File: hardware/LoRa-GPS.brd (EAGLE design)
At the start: 50.8 x 17.8 mm, 26 parts, among them J2 MF-CON-MICROUSB-RIGHT, U1 MCP1703-3302E/CB, Y1 CRYSTAL.ABS07

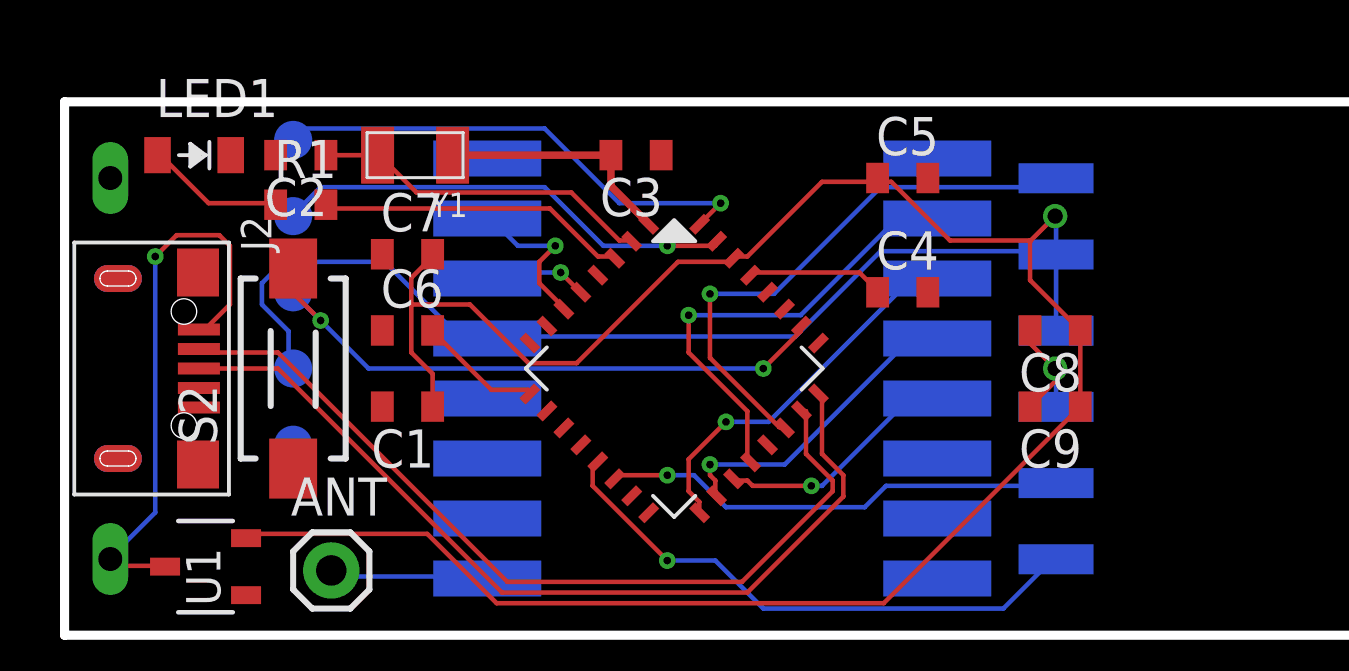
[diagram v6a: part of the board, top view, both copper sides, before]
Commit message: tidy GPS caps routing
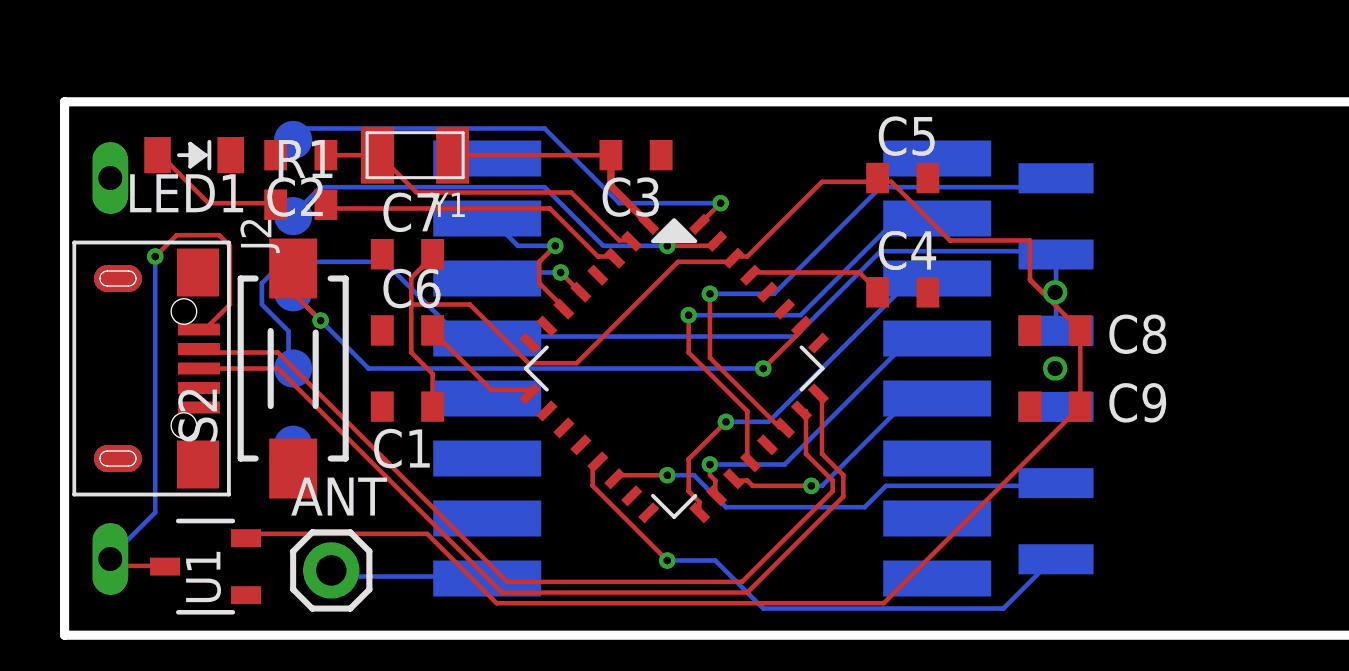
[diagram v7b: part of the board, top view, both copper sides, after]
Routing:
- net GND: track 4.54 -> 0.49 mm
- net VCC: track 105.8 -> 104.3 mm
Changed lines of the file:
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@@
 <layer number="23" name="tOrigins" color="15" fill="1" visible="yes" active="yes"/>
 <layer number="24" name="bOrigins" color="15" fill="1" visible="yes" active="yes"/>
-<layer number="25" name="tNames" color="7" fill="1" visible="no" active="yes"/>
+<layer number="25" name="tNames" color="7" fill="1" visible="yes" active="yes"/>
 <layer number="26" name="bNames" color="7" fill="1" visible="no" active="yes"/>
 <layer number="27" name="tValues" color="7" fill="1" visible="no" active="yes"/>
@@
 </element>
 <element name="LED1" library="nootropicdesign" package="CHIPLED_0805-THINCREAM" value="" x="4.318" y="16.002" smashed="yes" rot="R270">
-<attribute name="NAME" x="3.048" y="17.272" size="1.27" layer="25"/>
+<attribute name="NAME" x="2.032" y="14.097" size="1.27" layer="25"/>
 <attribute name="VALUE" x="3.048" y="13.462" size="1.27" layer="27"/>
 </element>
 <element name="C8" library="nootropicdesign" package="C0603-THINCREAM" value="10uF" x="33.02" y="10.16" smashed="yes" rot="R180">
-<attribute name="NAME" x="33.909" y="9.398" size="1.27" layer="25" rot="R180"/>
+<attribute name="NAME" x="36.83" y="10.668" size="1.27" layer="25" rot="R180"/>
 <attribute name="VALUE" x="33.909" y="12.192" size="1.27" layer="27" rot="R180"/>
 </element>
 <element name="C9" library="nootropicdesign" package="C0603-THINCREAM" value="100nF" x="33.02" y="7.62" smashed="yes" rot="R180">
-<attribute name="NAME" x="33.909" y="6.858" size="1.27" layer="25" rot="R180"/>
+<attribute name="NAME" x="36.83" y="8.382" size="1.27" layer="25" rot="R180"/>
 <attribute name="VALUE" x="33.909" y="9.652" size="1.27" layer="27" rot="R180"/>
 </element>
@@
 </polygon>
 <wire x1="32.1818" y1="10.16" x2="32.1818" y2="9.7282" width="0.1524" layer="1"/>
-<wire x1="32.1818" y1="9.7282" x2="33.02" y2="8.89" width="0.1524" layer="1"/>
-<wire x1="33.02" y1="8.89" x2="33.02" y2="8.4582" width="0.1524" layer="1"/>
-<wire x1="33.02" y1="8.4582" x2="32.1818" y2="7.62" width="0.1524" layer="1"/>
 <wire x1="33.02" y1="8.89" x2="33.05" y2="8.86" width="0.1524" layer="16"/>
-<wire x1="33.05" y1="8.86" x2="33.05" y2="7.61" width="0.1524" layer="16"/>
 </signal>
 <signal name="VCC">
@@
 <contactref element="SAMD21" pad="30"/>
 <contactref element="TP2" pad="P$1"/>
-<wire x1="33.02" y1="13.97" x2="32.1818" y2="13.1318" width="0.1524" layer="1"/>
-<via x="33.02" y="13.97" extent="1-16" drill="0.508"/>
-<wire x1="33.02" y1="13.97" x2="33.05" y2="13.94" width="0.254" layer="16"/>
-<wire x1="33.05" y1="13.94" x2="33.05" y2="12.69" width="0.1524" layer="16"/>
-<wire x1="33.05" y1="12.69" x2="33.05" y2="10.15" width="0.1524" layer="16"/>
+<wire x1="33.02" y1="11.43" x2="32.6136" y2="11.43" width="0.1524" layer="1"/>
+<wire x1="32.6136" y1="11.43" x2="32.1818" y2="11.8618" width="0.1524" layer="1"/>
+<via x="33.02" y="11.43" extent="1-16" drill="0.508"/>
+<wire x1="33.05" y1="11.46" x2="33.02" y2="11.43" width="0.254" layer="16"/>
 <wire x1="12.2682" y1="8.7122" x2="12.2682" y2="7.62" width="0.1524" layer="1"/>
 <wire x1="11.557" y1="9.4234" x2="12.2682" y2="8.7122" width="0.1524" layer="1"/>
@@
 <wire x1="32.1818" y1="13.1572" x2="29.5148" y2="13.1572" width="0.1524" layer="1"/>
 <wire x1="27.2034" y1="15.113" x2="27.1018" y2="15.24" width="0.1524" layer="1"/>
-<wire x1="32.1818" y1="13.1572" x2="32.1818" y2="13.1318" width="0.1524" layer="1"/>
-<wire x1="32.1818" y1="13.1318" x2="32.1818" y2="11.8364" width="0.1524" layer="1"/>
+<wire x1="32.1818" y1="11.8364" x2="32.1818" y2="11.8618" width="0.1524" layer="1"/>
+<wire x1="32.1818" y1="13.1572" x2="32.1818" y2="11.8618" width="0.1524" layer="1"/>
 <wire x1="32.1818" y1="11.8364" x2="33.8582" y2="10.16" width="0.1524" layer="1"/>
 <wire x1="27.305" y1="1.0668" x2="33.8582" y2="7.62" width="0.1524" layer="1"/>
 <wire x1="33.8582" y1="7.62" x2="33.8582" y2="10.16" width="0.1524" layer="1"/>
+<wire x1="33.05" y1="12.69" x2="33.05" y2="11.46" width="0.1524" layer="16"/>
+<wire x1="33.02" y1="11.43" x2="33.05" y2="11.4" width="0.1524" layer="16"/>
+<wire x1="33.05" y1="11.4" x2="33.05" y2="10.15" width="0.1524" layer="16"/>
 </signal>
 <signal name="VIN">
@@
 <wire x1="19.3802" y1="13.8684" x2="19.45505625" y2="13.728909375" width="0.1524" layer="1"/>
 <wire x1="19.45505625" y1="13.728909375" x2="19.47146875" y2="13.698325" width="0.1524" layer="1"/>
-<wire x1="12.934" y1="16.002" x2="18.2118" y2="16.002" width="0.254" layer="1"/>
+<wire x1="12.934" y1="16.002" x2="18.2118" y2="16.002" width="0.1524" layer="1"/>
 <wire x1="18.2118" y1="16.002" x2="18.2118" y2="14.972165625" width="0.254" layer="1"/>
 <wire x1="18.2118" y1="14.972165625" x2="19.45505625" y2="13.728909375" width="0.254" layer="1"/>

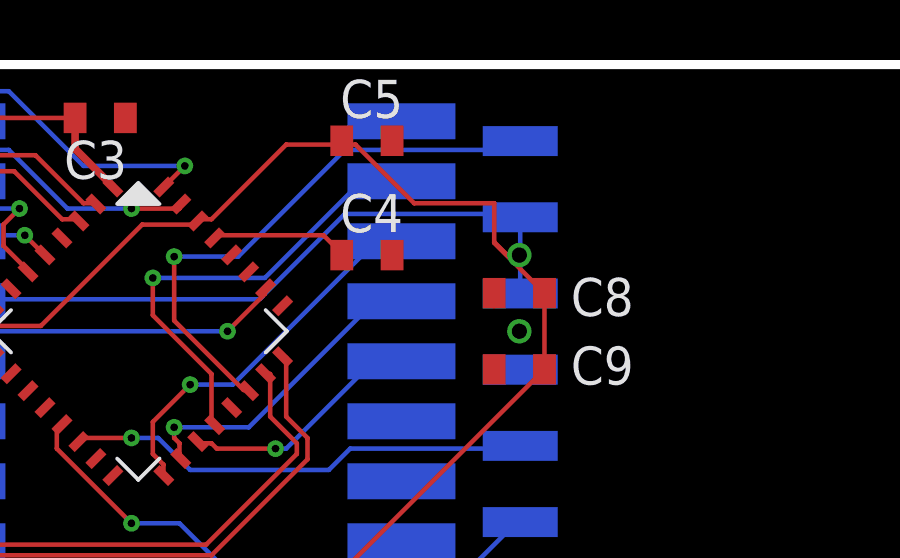
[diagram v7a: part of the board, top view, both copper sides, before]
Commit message: all vias 0.01
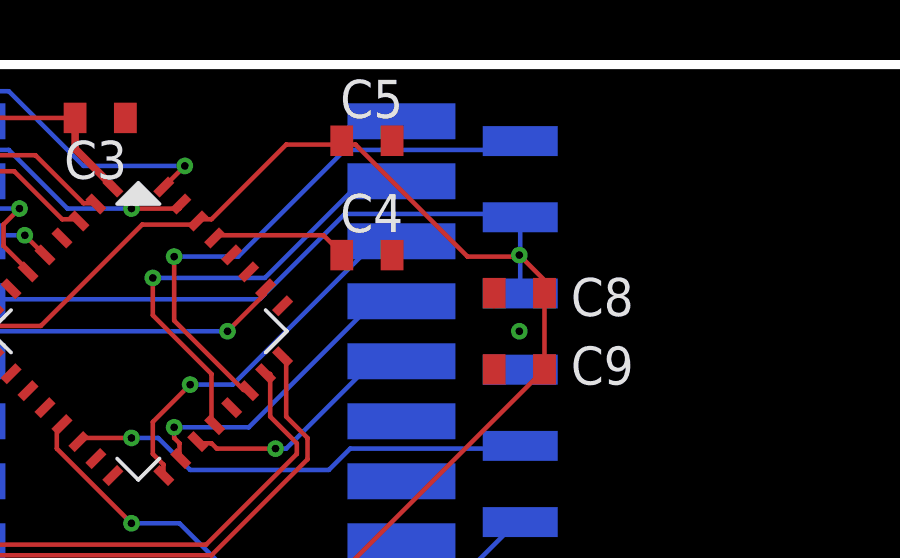
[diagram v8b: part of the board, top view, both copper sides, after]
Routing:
- net VCC: track 104.3 -> 102.8 mm
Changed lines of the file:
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@@
 <layer number="23" name="tOrigins" color="15" fill="1" visible="yes" active="yes"/>
 <layer number="24" name="bOrigins" color="15" fill="1" visible="yes" active="yes"/>
-<layer number="25" name="tNames" color="7" fill="1" visible="yes" active="yes"/>
+<layer number="25" name="tNames" color="7" fill="1" visible="no" active="yes"/>
 <layer number="26" name="bNames" color="7" fill="1" visible="no" active="yes"/>
 <layer number="27" name="tValues" color="7" fill="1" visible="no" active="yes"/>
@@
 <contactref element="SAMD21" pad="28"/>
 <contactref element="TP1" pad="P$1"/>
-<via x="33.02" y="8.89" extent="1-16" drill="0.508"/>
+<via x="33.02" y="8.89" extent="1-16" drill="0.254"/>
 <wire x1="33.02" y1="8.89" x2="33.01" y2="8.88" width="0.254" layer="16"/>
 <polygon width="0.254" layer="16">
@@
 <contactref element="SAMD21" pad="30"/>
 <contactref element="TP2" pad="P$1"/>
-<wire x1="33.02" y1="11.43" x2="32.6136" y2="11.43" width="0.1524" layer="1"/>
-<wire x1="32.6136" y1="11.43" x2="32.1818" y2="11.8618" width="0.1524" layer="1"/>
-<via x="33.02" y="11.43" extent="1-16" drill="0.508"/>
+<via x="33.02" y="11.43" extent="1-16" drill="0.254"/>
 <wire x1="33.05" y1="11.46" x2="33.02" y2="11.43" width="0.254" layer="16"/>
 <wire x1="12.2682" y1="8.7122" x2="12.2682" y2="7.62" width="0.1524" layer="1"/>
@@
 <wire x1="32.893" y1="12.8016" x2="33.05" y2="12.69" width="0.1524" layer="16"/>
 <wire x1="27.559" y1="15.113" x2="27.2034" y2="15.113" width="0.1524" layer="1"/>
-<wire x1="29.5148" y1="13.1572" x2="27.559" y2="15.113" width="0.1524" layer="1"/>
-<wire x1="32.1818" y1="13.1572" x2="29.5148" y2="13.1572" width="0.1524" layer="1"/>
+<wire x1="27.559" y1="15.113" x2="31.2928" y2="11.3792" width="0.1524" layer="1"/>
 <wire x1="27.2034" y1="15.113" x2="27.1018" y2="15.24" width="0.1524" layer="1"/>
-<wire x1="32.1818" y1="11.8364" x2="32.1818" y2="11.8618" width="0.1524" layer="1"/>
-<wire x1="32.1818" y1="13.1572" x2="32.1818" y2="11.8618" width="0.1524" layer="1"/>
-<wire x1="32.1818" y1="11.8364" x2="33.8582" y2="10.16" width="0.1524" layer="1"/>
 <wire x1="27.305" y1="1.0668" x2="33.8582" y2="7.62" width="0.1524" layer="1"/>
 <wire x1="33.8582" y1="7.62" x2="33.8582" y2="10.16" width="0.1524" layer="1"/>
@@
 <wire x1="33.02" y1="11.43" x2="33.05" y2="11.4" width="0.1524" layer="16"/>
 <wire x1="33.05" y1="11.4" x2="33.05" y2="10.15" width="0.1524" layer="16"/>
+<wire x1="31.2928" y1="11.3792" x2="32.9692" y2="11.3792" width="0.1524" layer="1"/>
+<wire x1="32.9692" y1="11.3792" x2="33.02" y2="11.43" width="0.1524" layer="1"/>
+<wire x1="33.02" y1="11.43" x2="33.8582" y2="10.5918" width="0.1524" layer="1"/>
+<wire x1="33.8582" y1="10.5918" x2="33.8582" y2="10.16" width="0.1524" layer="1"/>
 </signal>
 <signal name="VIN">
